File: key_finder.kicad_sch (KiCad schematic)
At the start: 27 parts, among them J1 Conn_ARM_JTAG_SWD_10, SW1 SW_Push, SW2 SW_Push, U1 NRF52832, X1 32MHz, X2 32.768kHz

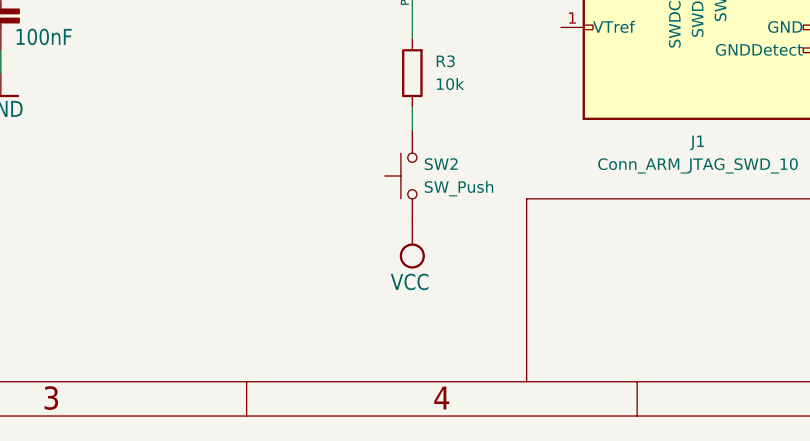
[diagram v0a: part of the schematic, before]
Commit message: change battery + relier les composants
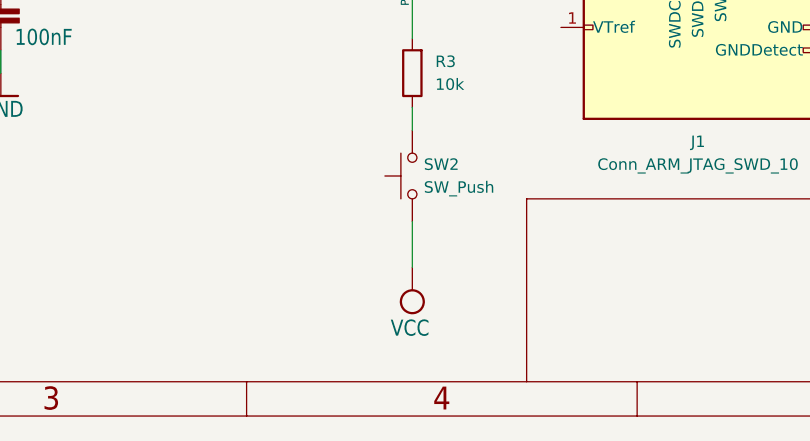
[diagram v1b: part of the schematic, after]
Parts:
- BT1: footprint Battery:BatteryHolder_Keystone_103_1x20mm -> Battery:BatteryHolder_Keystone_1057_1x2032; PRM 1057TR -> 36-1057-ND
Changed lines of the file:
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@@
     (stroke (width 0.1524) (type solid))
+  )
+  (wire (pts (xy 152.4 181.61) (xy 152.4 176.53))
+    (stroke (width 0) (type default))
   )
   (wire (pts (xy 162.56 71.12) (xy 162.56 73.66))
@@
         (path "/19671045-12a7-4138-bcff-fe62707deb04"
           (reference "C11") (unit 1)
+        )
+      )
+    )
+  )
+  (symbol (lib_id "key_finder-eagle-import:VCC") (at 152.4 184.15 180) (unit 1)
+    (in_bom yes) (on_board yes) (dnp no)
+    (property "Reference" "#VDD_NRF04" (at 152.4 184.15 0)
+      (effects (font (size 1.27 1.27)) hide)
+    )
+    (property "Value" "VCC" (at 154.305 187.325 0)
+      (effects (font (size 1.778 1.5113)) (justify left bottom))
+    )
+    (property "Footprint" "" (at 152.4 184.15 0)
+      (effects (font (size 1.27 1.27)) hide)
+    )
+    (property "Datasheet" "" (at 152.4 184.15 0)
+      (effects (font (size 1.27 1.27)) hide)
+    )
+    (pin "1")
+    (instances
+      (project "key_finder"
+        (path "/19671045-12a7-4138-bcff-fe62707deb04"
+          (reference "#VDD_NRF04") (unit 1)
         )
       )
@@
       (effects (font (size 1.27 1.27)) (justify left))
     )
-    (property "Footprint" "Battery:BatteryHolder_Keystone_103_1x20mm" (at 62.23 44.196 90)
+    (property "Footprint" "Battery:BatteryHolder_Keystone_1057_1x2032" (at 62.23 44.196 90)
       (effects (font (size 1.27 1.27)) hide)
     )
@@
       (effects (font (size 1.27 1.27)) hide)
     )
-    (property "PRM" "1057TR" (at 62.23 45.72 0)
+    (property "PRM" "36-1057-ND" (at 62.23 45.72 0)
       (effects (font (size 1.27 1.27)) hide)
     )
@@
         )
       )
-    )
-  )
-  (symbol (lib_id "key_finder-eagle-import:VCC") (at 152.4 179.07 180) (unit 1)
-    (in_bom yes) (on_board yes) (dnp no)
-    (property "Reference" "#VDD_NRF04" (at 152.4 179.07 0)
-      (effects (font (size 1.27 1.27)) hide)
-    )
-    (property "Value" "VCC" (at 154.305 182.245 0)
-      (effects (font (size 1.778 1.5113)) (justify left bottom))
-    )
-    (property "Footprint" "" (at 152.4 179.07 0)
-      (effects (font (size 1.27 1.27)) hide)
-    )
-    (property "Datasheet" "" (at 152.4 179.07 0)
-      (effects (font (size 1.27 1.27)) hide)
-    )
-    (pin "1")
-    (instances
-      (project "key_finder"
-        (path "/19671045-12a7-4138-bcff-fe62707deb04"
-          (reference "#VDD_NRF04") (unit 1)
-        )
-      )

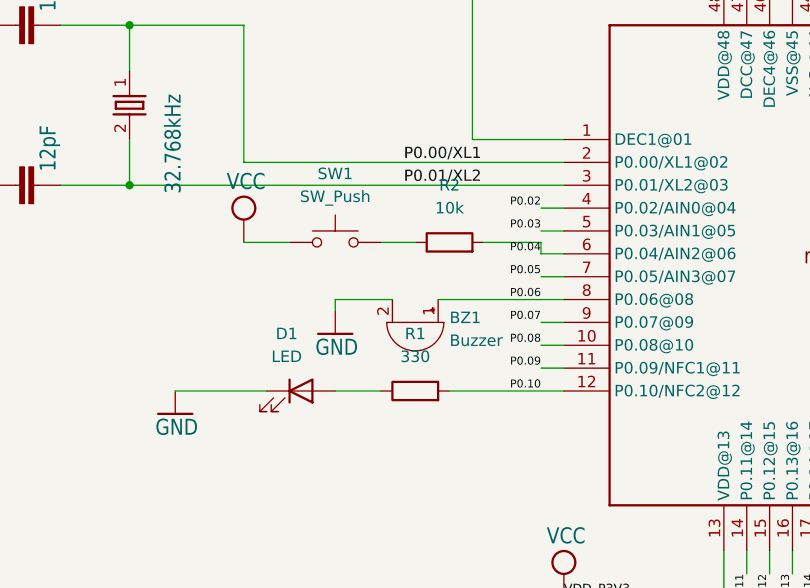
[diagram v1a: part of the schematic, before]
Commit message: correct som ref and add readme
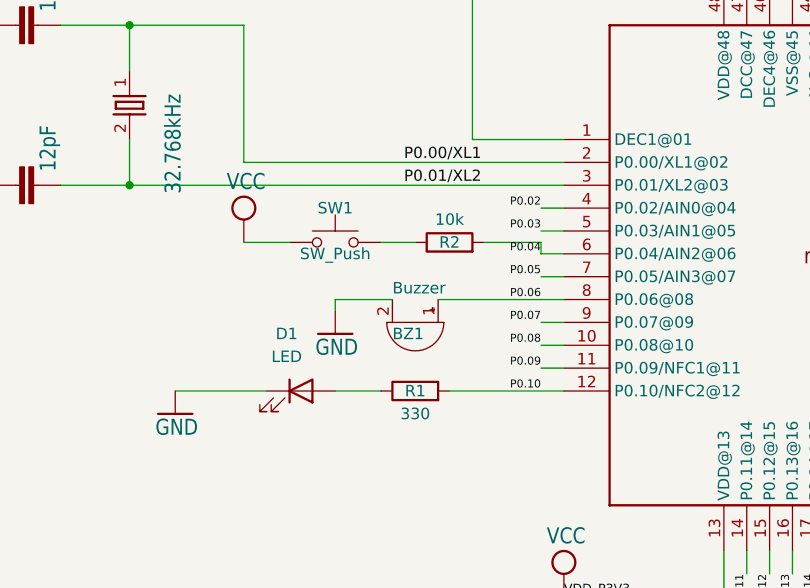
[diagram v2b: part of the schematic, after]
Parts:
- BZ1: PRM BUZZER PIEZO 3V 9X9MM SMD -> SMT-0940-T-3V-R
- SW2: PRM SWITCH TACTILE SPST-NO 0.05A 32V -> KMR223GLFG
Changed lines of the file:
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@@
   )
   (symbol (lib_id "Device:Buzzer") (at 90.17 116.84 270) (unit 1)
-    (in_bom yes) (on_board yes) (dnp no) (fields_autoplaced)
-    (property "Reference" "BZ1" (at 93.98 116.3251 90)
+    (in_bom yes) (on_board yes) (dnp no)
+    (property "Reference" "BZ1" (at 87.63 118.11 90)
       (effects (font (size 1.27 1.27)) (justify left))
     )
-    (property "Value" "Buzzer" (at 93.98 118.8651 90)
+    (property "Value" "Buzzer" (at 87.63 113.03 90)
       (effects (font (size 1.27 1.27)) (justify left))
     )
@@
       (effects (font (size 1.27 1.27)) hide)
     )
-    (property "PRM" "BUZZER PIEZO 3V 9X9MM SMD" (at 90.17 116.84 90)
+    (property "PRM" "SMT-0940-T-3V-R" (at 90.17 116.84 90)
       (effects (font (size 1.27 1.27)) hide)
     )
@@
   )
   (symbol (lib_id "Switch:SW_Push") (at 81.28 107.95 0) (unit 1)
-    (in_bom yes) (on_board yes) (dnp no) (fields_autoplaced)
-    (property "Reference" "SW1" (at 81.28 100.33 0)
+    (in_bom yes) (on_board yes) (dnp no)
+    (property "Reference" "SW1" (at 81.28 104.14 0)
       (effects (font (size 1.27 1.27)))
     )
-    (property "Value" "SW_Push" (at 81.28 102.87 0)
+    (property "Value" "SW_Push" (at 81.28 109.22 0)
       (effects (font (size 1.27 1.27)))
     )
@@
       (effects (font (size 1.27 1.27)) hide)
     )
-    (property "PRM" "SWITCH TACTILE SPST-NO 0.05A 32V" (at 152.4 171.45 90)
+    (property "PRM" "KMR223GLFG" (at 152.4 171.45 90)
       (effects (font (size 1.27 1.27)) hide)
     )
@@
   )
   (symbol (lib_id "Device:R") (at 93.98 107.95 90) (unit 1)
-    (in_bom yes) (on_board yes) (dnp no) (fields_autoplaced)
-    (property "Reference" "R2" (at 93.98 101.6 90)
+    (in_bom yes) (on_board yes) (dnp no)
+    (property "Reference" "R2" (at 93.98 107.95 90)
       (effects (font (size 1.27 1.27)))
     )
-    (property "Value" "10k" (at 93.98 104.14 90)
+    (property "Value" "10k" (at 93.98 105.41 90)
       (effects (font (size 1.27 1.27)))
     )
@@
   )
   (symbol (lib_id "Device:R") (at 90.17 124.46 90) (unit 1)
-    (in_bom yes) (on_board yes) (dnp no) (fields_autoplaced)
-    (property "Reference" "R1" (at 90.17 118.11 90)
+    (in_bom yes) (on_board yes) (dnp no)
+    (property "Reference" "R1" (at 90.17 124.46 90)
       (effects (font (size 1.27 1.27)))
     )
-    (property "Value" "330" (at 90.17 120.65 90)
+    (property "Value" "330" (at 90.17 127 90)
       (effects (font (size 1.27 1.27)))
     )

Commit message: sceance 2
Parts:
- added MK1: Microphone, Sensor_Audio:CUI_CMC-4013-SMT, symbol Device:Microphone
- BT1: footprint Battery:BatteryHolder_Keystone_1057_1x2032 -> Battery:BatteryHolder_Keystone_1060_1x2032; PRM 36-1057-ND -> 36-1060-ND
- SW1: footprint Button_Switch_THT:SW_PUSH_6mm_H7.3mm -> Button_Switch_SMD:SW_Push_1P1T_NO_CK_KMR2; PRM TS04-66-50-BK-160-SMT -> KMR223GLFG
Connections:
- net P0.09: now also R1.2
- net P0.10: now also MK1.1 (-); no longer R1.2
- net VCC: now also MK1.2 (+)
- net P0.00/XL1: no longer names the net of C11.2, U1.2 (P0.00/XL1@02), X2.1
- net P0.01/XL2: no longer names the net of C12.2, U1.3 (P0.01/XL2@03), X2.2
